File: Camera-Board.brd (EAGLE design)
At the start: 100.3 x 64.8 mm, 65 parts, among them J1 RJ45KEYSTONE-942, J2 JTAG_ARM_10PIN, J3 APP_2POS_CONFIG12V_HORIZ, J8 APPPP45_PCB_HORIZ_RIGHT, U1 TM4C1294NCPDT, U2 HX1198FNL, U3 SLVU2.8-4, U4 OKI-78SR-5/1.5-W36HC, U5 TPS73733DCQ, U7 OKI-78SR-5/1.5-W36HC, Y1 NX3225GA, Y2 CRYATL_32K_SMD

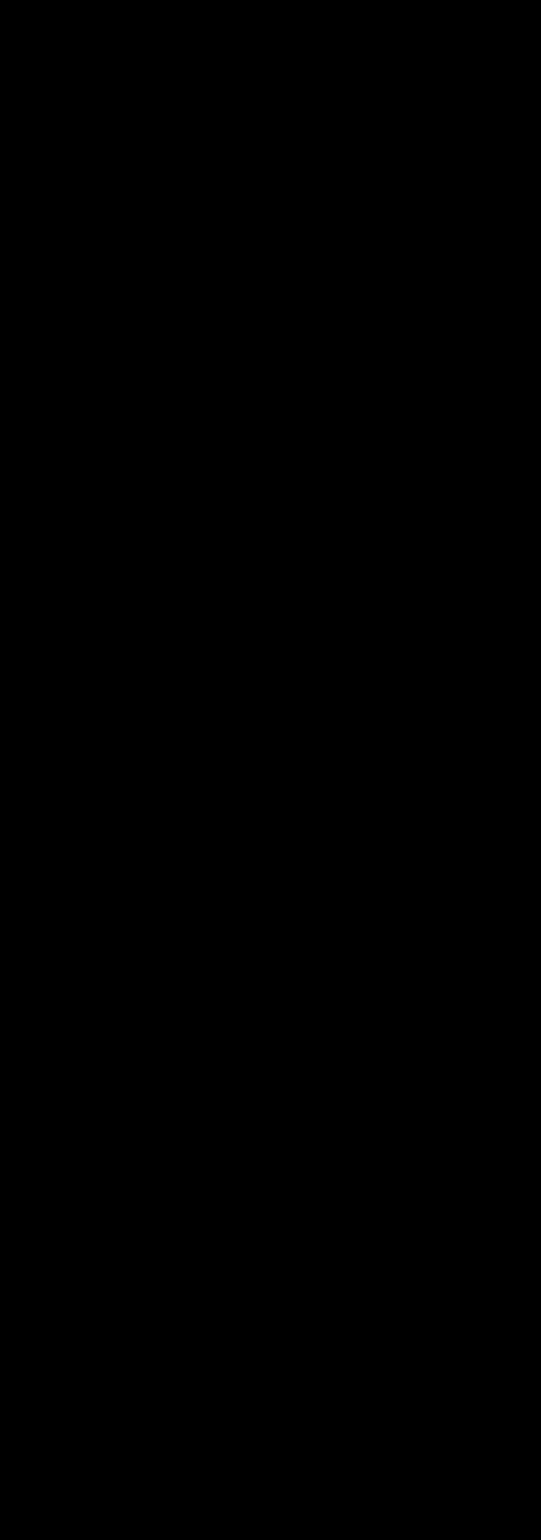
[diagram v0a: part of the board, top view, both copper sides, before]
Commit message: Added Max4312 chip to schematic
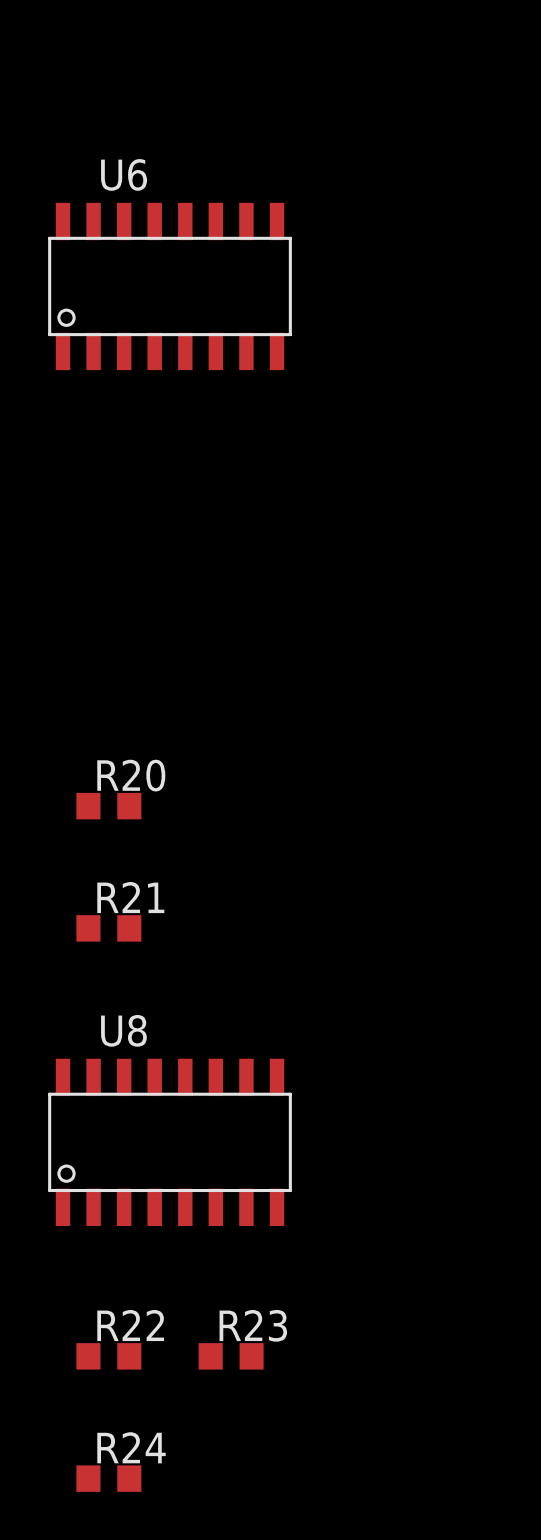
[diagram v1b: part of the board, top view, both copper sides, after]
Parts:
- added R20, R21, R22, R23: 500, resistor:R0603
- added R24: 75, resistor:R0603
- added U6, U8: MAX4312ESE, MRDT-ICs:SOIC16
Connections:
- new net CAM_IN0: R24.2, U6.5, U8.5
- new net CAM_IN1: U6.6, U8.6
- new net CAM_IN2: U6.7, U8.7
- new net CAM_IN3: U6.8, U8.8
- new net CAM_IN4: U6.9, U8.9
- new net CAM_IN5: U6.10, U8.10
- new net CAM_IN6: U6.11, U8.11
- new net CAM_IN7: U6.12, U8.12
- new net CAM_OUT0: R20.2, U6.16
- new net CAM_OUT1: R22.2, U8.16
- new net MUX0_0: U6.3
- new net MUX0_1: U6.2
- new net MUX0_2: U6.1
- new net MUX0_SHDN: U6.14
- new net MUX1_0: U8.3
- new net MUX1_1: U8.2
- new net MUX1_2: U8.1
- new net MUX1_SHDN: U8.14
- new net N$1: R20.1, R21.2, U6.15
- new net N$2: R22.1, R23.2, U8.15
- net +5V_LOGIC: now also U6.4, U8.4
- net GND: now also R21.1, R23.1, R24.1, U6.13, U8.13
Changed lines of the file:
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@@
 <element name="C25" library="resistor" package="C1206" value="10uF" x="24.765" y="7.3025" rot="R90"/>
 <element name="C26" library="resistor" package="C1206" value="10uF" x="24.765" y="13.97" rot="R90"/>
+<element name="U6" library="MRDT-ICs" package="SOIC16" value="MAX4312ESE" x="-21.59" y="-13.97"/>
+<element name="R20" library="resistor" package="R0603" value="500" x="-24.13" y="-35.56"/>
+<element name="R21" library="resistor" package="R0603" value="500" x="-24.13" y="-40.64"/>
+<element name="U8" library="MRDT-ICs" package="SOIC16" value="MAX4312ESE" x="-21.59" y="-49.53"/>
+<element name="R22" library="resistor" package="R0603" value="500" x="-24.13" y="-58.42"/>
+<element name="R23" library="resistor" package="R0603" value="500" x="-19.05" y="-58.42"/>
+<element name="R24" library="resistor" package="R0603" value="75" x="-24.13" y="-63.5"/>
 </elements>
 <signals>
@@
 <via x="21.59" y="15.24" extent="1-16" drill="0.6" shape="square"/>
 <via x="21.59" y="8.89" extent="1-16" drill="0.6" shape="square"/>
+<contactref element="U6" pad="13"/>
+<contactref element="R21" pad="1"/>
+<contactref element="U8" pad="13"/>
+<contactref element="R23" pad="1"/>
+<contactref element="R24" pad="1"/>
+<wire x1="59.3725" y1="58.7375" x2="59.3725" y2="60.96" width="0" layer="19" extent="1-1"/>
+<wire x1="59.3725" y1="56.515" x2="59.3725" y2="58.7375" width="0" layer="19" extent="1-1"/>
+<wire x1="63.08" y1="50.8" x2="59.3725" y2="56.515" width="0" layer="19" extent="1-1"/>
+<wire x1="61.2775" y1="46.99" x2="63.08" y2="50.8" width="0" layer="19" extent="1-1"/>
+<wire x1="57.704515625" y1="47.70548125" x2="59.6844125" y2="45.725584375" width="0" layer="19" extent="1-1"/>
+<wire x1="56.916225" y1="38.4175" x2="59.6844125" y2="45.725584375" width="0" layer="19" extent="1-1"/>
+<wire x1="63.08" y1="33.02" x2="58.2702" y2="37.063525" width="0" layer="19" extent="1-1"/>
+<wire x1="64.6675" y1="35.56" x2="64.4525" y2="33.02" width="0" layer="19" extent="1-1"/>
+<wire x1="64.6675" y1="37.7825" x2="64.6675" y2="35.56" width="0" layer="19" extent="1-1"/>
+<wire x1="62.23" y1="25.4" x2="63.08" y2="33.02" width="0" layer="19" extent="1-1"/>
+<wire x1="60.96" y1="25.4" x2="62.23" y2="25.4" width="0" layer="19" extent="1-1"/>
+<wire x1="49.53" y1="60.0075" x2="58" y2="60.96" width="0" layer="19" extent="1-1"/>
+<wire x1="49.53" y1="57.785" x2="49.53" y2="60.0075" width="0" layer="19" extent="1-1"/>
+<wire x1="49.53" y1="55.5625" x2="49.53" y2="57.785" width="0" layer="19" extent="1-1"/>
+<wire x1="43.18" y1="59.3725" x2="48.1575" y2="60.0075" width="0" layer="19" extent="1-1"/>
+<wire x1="38.4175" y1="62.5475" x2="42.193540625" y2="58.45395625" width="0" layer="19" extent="1-1"/>
+<wire x1="45.72" y1="49.2125" x2="48.1575" y2="55.5625" width="0" layer="19" extent="1-1"/>
+<wire x1="45.082659375" y1="45.725584375" x2="47.062559375" y2="47.70548125" width="0" layer="19" extent="1-1"/>
+<wire x1="38.0755" y1="47.3075" x2="44.23413125" y2="44.87705625" width="0" layer="19" extent="1-1"/>
+<wire x1="32.301515625" y1="48.5775" x2="36.5125" y2="48.26" width="0" layer="19" extent="1-1"/>
+<wire x1="35.98" y1="42.2275" x2="37.465" y2="47.3075" width="0" layer="19" extent="1-1"/>
+<wire x1="34.925" y1="36.5125" x2="34.925" y2="41.5925" width="0" layer="19" extent="1-1"/>
+<wire x1="35.2425" y1="33.3375" x2="34.925" y2="36.5125" width="0" layer="19" extent="1-1"/>
+<wire x1="35.345" y1="29.21" x2="35.345" y2="31.4325" width="0" layer="19" extent="1-1"/>
+<wire x1="38.1" y1="33.02" x2="35.345" y2="33.235" width="0" layer="19" extent="1-1"/>
+<wire x1="45.4025" y1="35.56" x2="39.6875" y2="33.1225" width="0" layer="19" extent="1-1"/>
+<wire x1="43.18" y1="27.305" x2="39.6875" y2="33.1225" width="0" layer="19" extent="1-1"/>
+<wire x1="48.895" y1="28.79" x2="44.45" y2="27.09" width="0" layer="19" extent="1-1"/>
+<wire x1="20.7772" y1="39.9288" x2="29.3125" y2="46.355" width="0" layer="19" extent="1-1"/>
+<wire x1="17.78" y1="36.12" x2="20.7772" y2="38.2778" width="0" layer="19" extent="1-1"/>
+<wire x1="20.535" y1="26.9875" x2="17.78" y2="29.92" width="0" layer="19" extent="1-1"/>
+<wire x1="11.43" y1="43.18" x2="13.97" y2="39.9288" width="0" layer="19" extent="1-1"/>
+<wire x1="6.35" y1="43.18" x2="11.2425" y2="43.18" width="0" layer="19" extent="1-1"/>
+<wire x1="6.35" y1="40.64" x2="6.1625" y2="43.18" width="0" layer="19" extent="1-1"/>
+<wire x1="12.7" y1="33.655" x2="17.78" y2="33.02" width="0" layer="19" extent="1-1"/>
+<wire x1="13.12" y1="26.67" x2="17.78" y2="29.92" width="0" layer="19" extent="1-1"/>
+<wire x1="18.034" y1="20.701" x2="20.535" y2="26.9875" width="0" layer="19" extent="1-1"/>
+<wire x1="21.59" y1="15.37" x2="18.034" y2="20.701" width="0" layer="19" extent="1-1"/>
+<wire x1="21.59" y1="8.89" x2="21.59" y2="15.24" width="0" layer="19" extent="1-1"/>
+<wire x1="29.21" y1="8.89" x2="24.765" y2="8.7025" width="0" layer="19" extent="1-1"/>
+<wire x1="-22.225" y1="-11.27" x2="21.59" y2="8.7025" width="0" layer="19" extent="1-1"/>
+<wire x1="-24.98" y1="-40.64" x2="-22.225" y2="-11.27" width="0" layer="19" extent="1-1"/>
+<wire x1="-22.225" y1="-46.83" x2="-24.98" y2="-40.64" width="0" layer="19" extent="1-1"/>
+<wire x1="-19.9" y1="-58.42" x2="-22.225" y2="-46.83" width="0" layer="19" extent="1-1"/>
+<wire x1="-24.98" y1="-63.5" x2="-19.9" y2="-58.42" width="0" layer="19" extent="1-1"/>
 </signal>
 <signal name="+5V_ACT">
@@
 <vertex x="10.16" y="45.72"/>
 </polygon>
+<contactref element="U6" pad="4"/>
+<contactref element="U8" pad="4"/>
+<wire x1="-22.225" y1="-16.67" x2="-22.225" y2="-52.23" width="0" layer="19" extent="1-1"/>
+<wire x1="9.7675" y1="29.92" x2="-22.225" y2="-16.67" width="0" layer="19" extent="1-1"/>
+<wire x1="8.89" y1="40.64" x2="12.7" y2="30.9" width="0" layer="19" extent="1-1"/>
+<wire x1="8.4425" y1="43.18" x2="8.89" y2="40.64" width="0" layer="19" extent="1-1"/>
+</signal>
+<signal name="CAM_IN0">
+<contactref element="U6" pad="5"/>
+<contactref element="U8" pad="5"/>
+<contactref element="R24" pad="2"/>
+<wire x1="-20.955" y1="-52.23" x2="-23.28" y2="-63.5" width="0" layer="19" extent="1-1"/>
+<wire x1="-20.955" y1="-16.67" x2="-20.955" y2="-52.23" width="0" layer="19" extent="1-1"/>
+</signal>
+<signal name="CAM_IN1">
+<contactref element="U6" pad="6"/>
+<contactref element="U8" pad="6"/>
+<wire x1="-19.685" y1="-16.67" x2="-19.685" y2="-52.23" width="0" layer="19" extent="1-1"/>
+</signal>
+<signal name="CAM_IN2">
+<contactref element="U6" pad="7"/>
+<contactref element="U8" pad="7"/>
+<wire x1="-18.415" y1="-16.67" x2="-18.415" y2="-52.23" width="0" layer="19" extent="1-1"/>
+</signal>
+<signal name="CAM_IN3">
+<contactref element="U6" pad="8"/>
+<contactref element="U8" pad="8"/>
+<wire x1="-17.145" y1="-16.67" x2="-17.145" y2="-52.23" width="0" layer="19" extent="1-1"/>
+</signal>
+<signal name="CAM_IN4">
+<contactref element="U6" pad="9"/>
+<contactref element="U8" pad="9"/>
+<wire x1="-17.145" y1="-11.27" x2="-17.145" y2="-46.83" width="0" layer="19" extent="1-1"/>
+</signal>
+<signal name="CAM_IN5">
+<contactref element="U6" pad="10"/>
+<contactref element="U8" pad="10"/>
+<wire x1="-18.415" y1="-11.27" x2="-18.415" y2="-46.83" width="0" layer="19" extent="1-1"/>
+</signal>
+<signal name="CAM_IN6">
+<contactref element="U6" pad="11"/>
+<contactref element="U8" pad="11"/>
+<wire x1="-19.685" y1="-11.27" x2="-19.685" y2="-46.83" width="0" layer="19" extent="1-1"/>
+</signal>
+<signal name="CAM_IN7">
+<contactref element="U6" pad="12"/>
+<contactref element="U8" pad="12"/>
+<wire x1="-20.955" y1="-11.27" x2="-20.955" y2="-46.83" width="0" layer="19" extent="1-1"/>
+</signal>
+<signal name="CAM_OUT0">
+<contactref element="U6" pad="16"/>
+<contactref element="R20" pad="2"/>
+<wire x1="-26.035" y1="-11.27" x2="-23.28" y2="-35.56" width="0" layer="19" extent="1-1"/>
+</signal>
+<signal name="N$1">
+<contactref element="U6" pad="15"/>
+<contactref element="R20" pad="1"/>
+<contactref element="R21" pad="2"/>
+<wire x1="-24.98" y1="-35.56" x2="-23.28" y2="-40.64" width="0" layer="19" extent="1-1"/>
+<wire x1="-24.765" y1="-11.27" x2="-24.98" y2="-35.56" width="0" layer="19" extent="1-1"/>
+</signal>
+<signal name="N$2">
+<contactref element="U8" pad="15"/>
+<contactref element="R22" pad="1"/>
+<contactref element="R23" pad="2"/>
+<wire x1="-18.2" y1="-58.42" x2="-24.98" y2="-58.42" width="0" layer="19" extent="1-1"/>
+<wire x1="-24.765" y1="-46.83" x2="-24.98" y2="-58.42" width="0" layer="19" extent="1-1"/>
+</signal>
+<signal name="CAM_OUT1">
+<contactref element="U8" pad="16"/>
+<contactref element="R22" pad="2"/>
+<wire x1="-26.035" y1="-46.83" x2="-23.28" y2="-58.42" width="0" layer="19" extent="1-1"/>
+</signal>
+<signal name="MUX0_0">
+<contactref element="U6" pad="3"/>
+</signal>
+<signal name="MUX0_1">
+<contactref element="U6" pad="2"/>
+</signal>
+<signal name="MUX0_2">
+<contactref element="U6" pad="1"/>
+</signal>
+<signal name="MUX0_SHDN">
+<contactref element="U6" pad="14"/>
+</signal>
+<signal name="MUX1_SHDN">
+<contactref element="U8" pad="14"/>
+</signal>
+<signal name="MUX1_2">
+<contactref element="U8" pad="1"/>
+</signal>
+<signal name="MUX1_1">
+<contactref element="U8" pad="2"/>
+</signal>
+<signal name="MUX1_0">
+<contactref element="U8" pad="3"/>
 </signal>
 </signals>

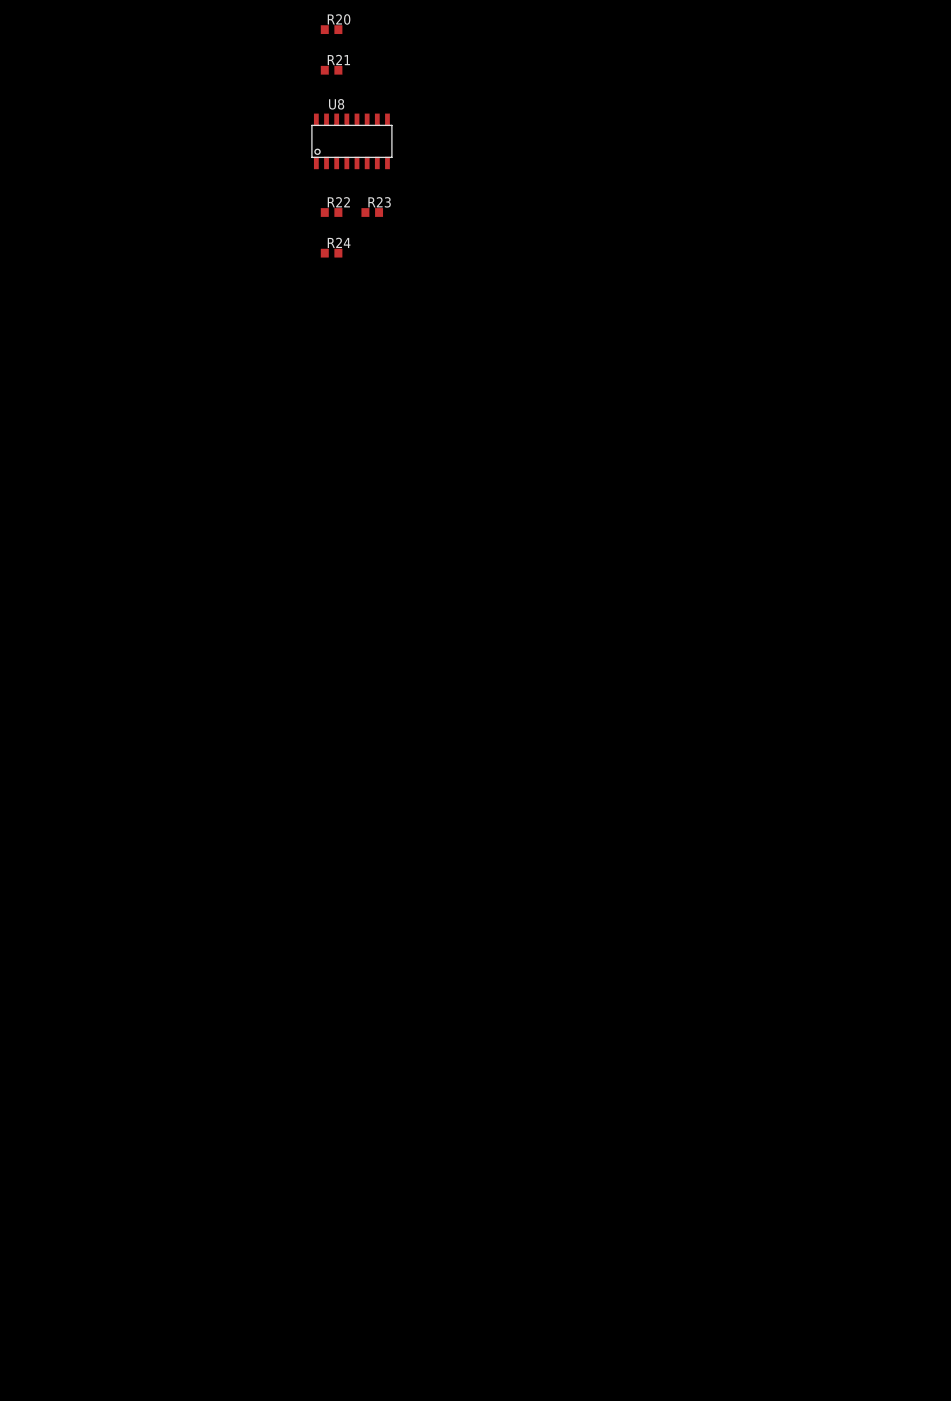
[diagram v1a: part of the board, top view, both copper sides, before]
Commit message: Added Input and Output Connectors
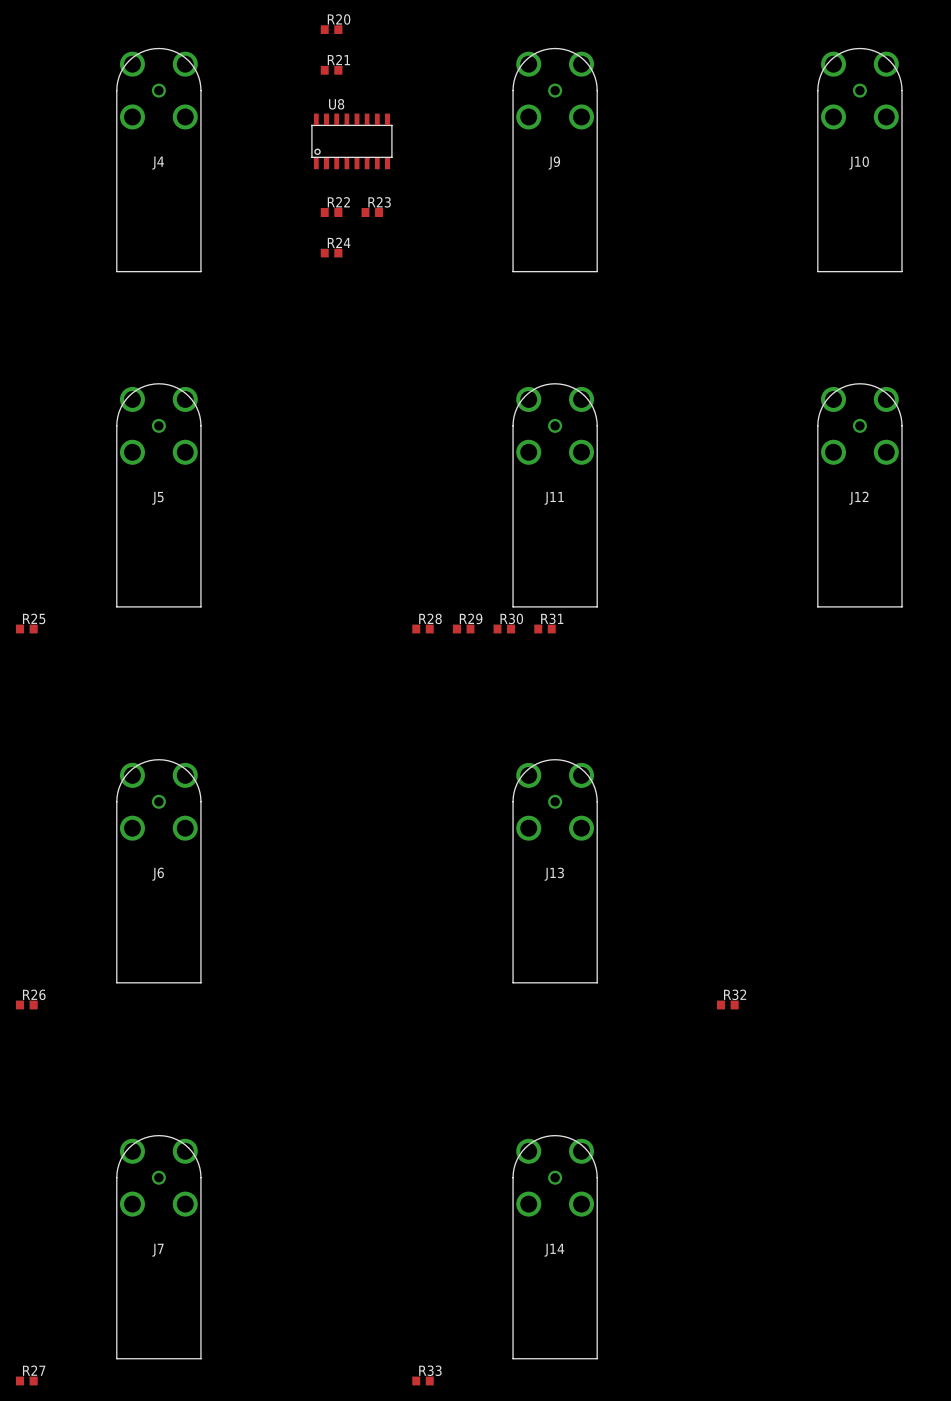
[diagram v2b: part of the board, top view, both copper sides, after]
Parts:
- added J10, J11, J12, J13, J14, J4, J5, J6, J7, J9: BNC, MRDT-Connectors:MOLEX-0731711640-BNC
- added R25, R26, R27, R28, R29, R30, R31, R32, R33: 75, resistor:R0603
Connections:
- new net N$3: J14.P$1, R33.1
- new net N$4: J13.P$1, R32.1
- net CAM_IN0: now also J4.P$1
- net CAM_IN1: now also J5.P$1, R25.2
- net CAM_IN2: now also J6.P$1, R26.2
- net CAM_IN3: now also J7.P$1, R27.2
- net CAM_IN4: now also J9.P$1, R28.2
- net CAM_IN5: now also J10.P$1, R29.2
- net CAM_IN6: now also J11.P$1, R30.2
- net CAM_IN7: now also J12.P$1, R31.2
- net CAM_OUT0: now also R32.2, R33.2
- net GND: now also J10.P$2, J10.P$3, J10.P$4, J10.P$5, J11.P$2, J11.P$3, J11.P$4, J11.P$5, J12.P$2, J12.P$3, J12.P$4, J12.P$5, J13.P$2, J13.P$3, J13.P$4, J13.P$5, J14.P$2, J14.P$3, J14.P$4, J14.P$5, J4.P$2, J4.P$3, J4.P$4, J4.P$5, J5.P$2, J5.P$3, J5.P$4, J5.P$5, J6.P$2, J6.P$3, J6.P$4, J6.P$5, J7.P$2, J7.P$3, J7.P$4, J7.P$5, J9.P$2, J9.P$3, J9.P$4, J9.P$5, R25.1, R26.1, R27.1, R28.1, R29.1, R30.1, R31.1

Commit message: Rotouted most connections
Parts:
- removed C25, C26: 10uF, resistor:C1206
- removed J8: APPPP45_PCB_HORIZ_RIGHT, MRDT-Connectors:APP45_PCB_HORIZ_RIGHT
- removed U7: OKI-78SR-5/1.5-W36HC, MRDT-ICs:OKI-78SR_HORIZ
- moved R27 286.3 mm to (69.8, 49.5), turned to 90 degrees
- moved J7 263.0 mm to (69.8, 57.1), turned to 180 degrees
- moved R33 259.6 mm to (108.0, 25.4), turned to 180 degrees
- moved R26 252.6 mm to (82.5, 49.5), turned to 90 degrees
- moved J14 233.0 mm to (115.6, 25.4), turned to 90 degrees
- moved J6 228.6 mm to (82.5, 57.1), turned to 180 degrees
- moved R25 224.5 mm to (95.2, 49.5), turned to 90 degrees
- moved R32 213.5 mm to (108.0, 39.4), turned to 180 degrees
- moved J13 204.7 mm to (115.6, 39.4), turned to 90 degrees
- moved J5 200.3 mm to (95.2, 57.1), turned to 180 degrees
- moved J4 183.5 mm to (108.0, 57.1), turned to 180 degrees
- moved R24 173.8 mm to (108.0, 49.5), turned to 90 degrees
- moved R31 164.1 mm to (108.0, 15.2), turned to 270 degrees
- moved R30 159.3 mm to (95.2, 15.2), turned to 270 degrees
- moved R29 154.7 mm to (82.5, 15.2), turned to 270 degrees
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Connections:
- removed net +12V_ACT: C25.1, J8.P$1, U7.1
- removed net +5V_ACT: C26.1, U7.3
- net CAM_OUT0: no longer R33.2
- net CAM_OUT1: now also R33.2
- net GND: no longer C25.2, C26.2, U7.2
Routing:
- net +5V_LOGIC: track 20.2 -> 131.9 mm, vias 2 -> 5
- net CAM_IN0: track 0.00 -> 59.4 mm, vias 0 -> 2
- net CAM_IN4: track 0.00 -> 54.3 mm, vias 0 -> 2
- net CAM_IN7: track 0.00 -> 53.8 mm, vias 0 -> 2
- net CAM_IN3: track 0.00 -> 52.0 mm, vias 0 -> 2
- net CAM_IN1: track 0.00 -> 47.3 mm, vias 0 -> 2
- net CAM_IN6: track 0.00 -> 45.0 mm, vias 0 -> 2
- net CAM_IN2: track 0.00 -> 43.1 mm, vias 0 -> 2
- net CAM_IN5: track 0.00 -> 42.8 mm, vias 0 -> 2
- net N$4: track 0.00 -> 6.77 mm
- net N$3: track 0.00 -> 6.77 mm
- net N$2: track 0.00 -> 6.28 mm
- net N$1: track 0.00 -> 6.28 mm
- net CAM_OUT1: track 0.00 -> 3.74 mm
- net CAM_OUT0: track 0.00 -> 3.74 mm
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- removed copper zone on layer 1, net +12V_ACT
- removed copper zone on layer 1, net +5V_ACT
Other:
- board size 100.3 x 64.8 mm -> 123.2 x 64.8 mm
